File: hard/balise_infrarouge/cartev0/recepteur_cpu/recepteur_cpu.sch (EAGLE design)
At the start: 14 parts, among them U1 ARDUINO_SHIELDNO_SILK

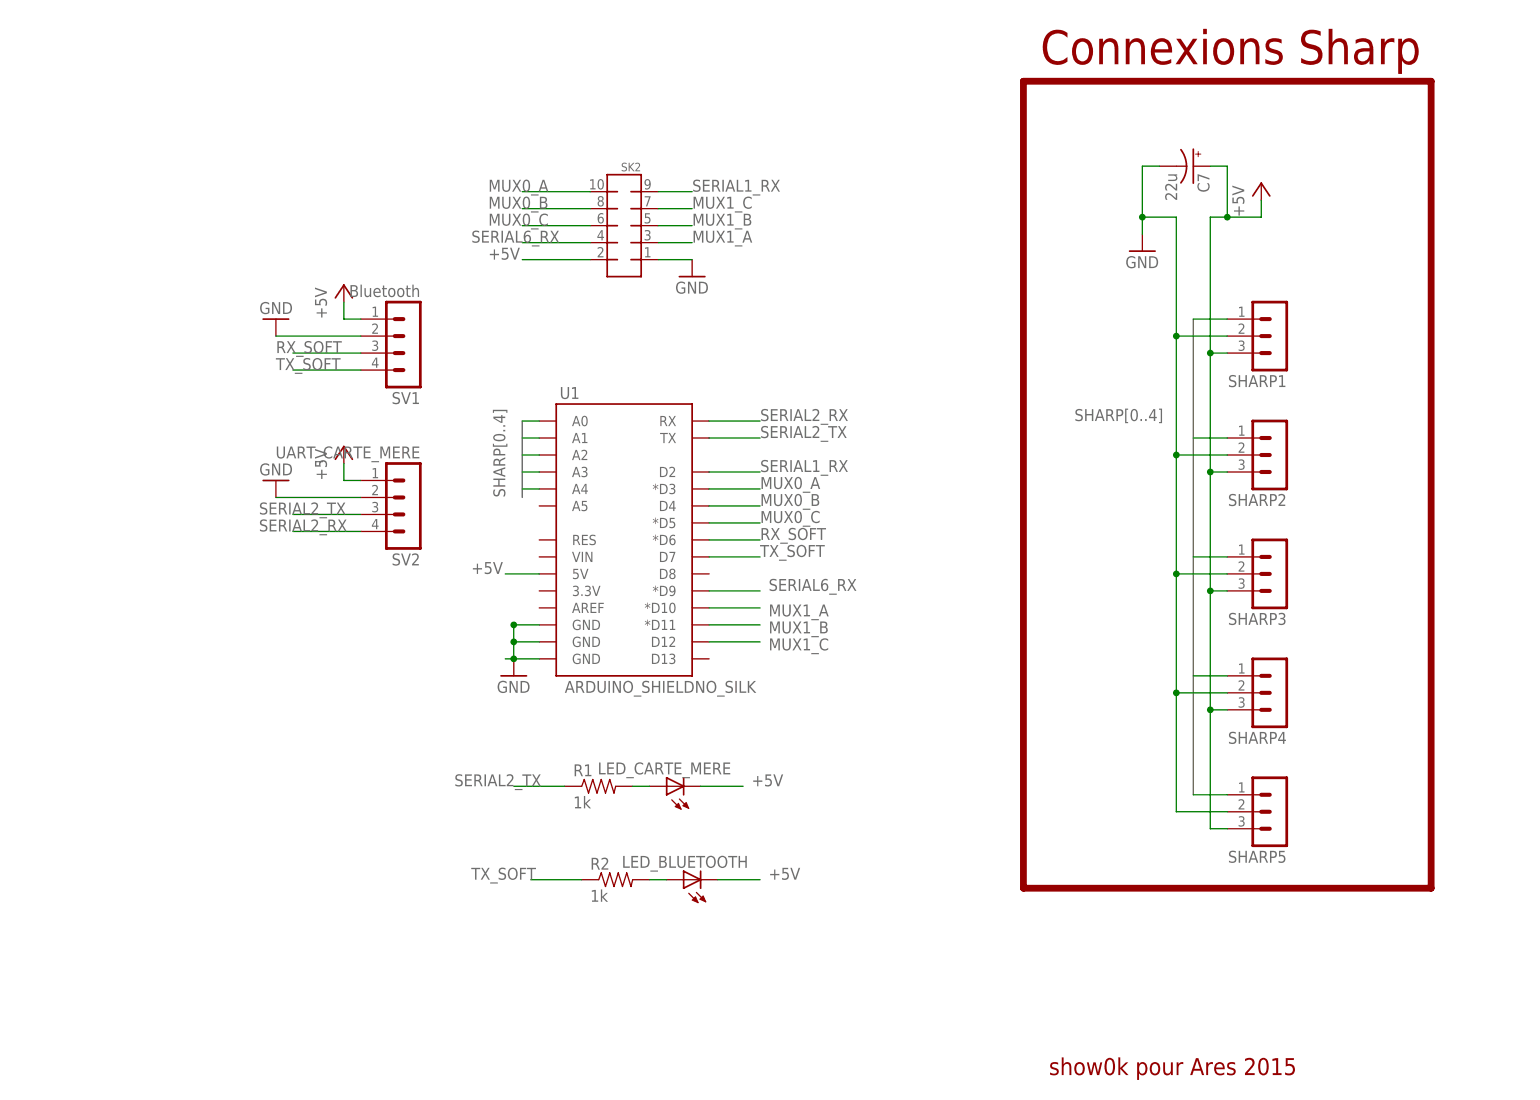
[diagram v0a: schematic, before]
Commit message: maj carte extension nucleo
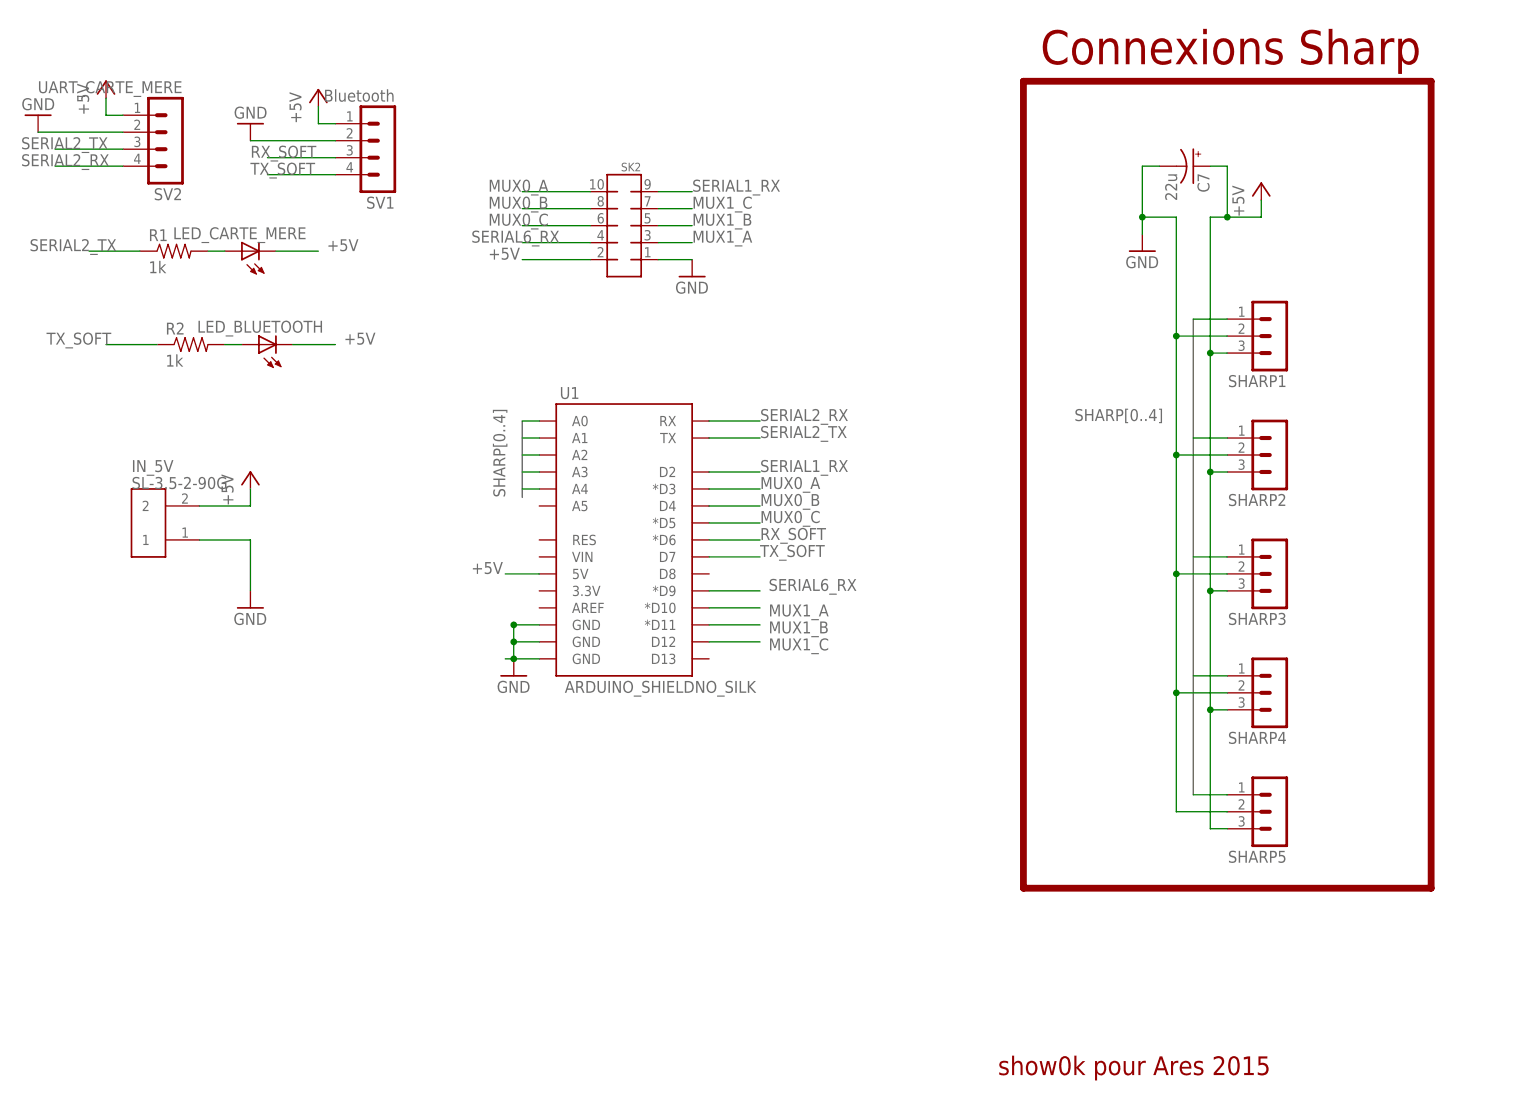
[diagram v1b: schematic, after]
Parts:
- added IN_5V: SL-3.5-2-90G, WEIDMULLER:SL-3.5-2-90G
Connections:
- net +5V: now also IN_5V.2
- net GND: now also IN_5V.1
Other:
- moved on the sheet: LED_BLUETOOTH, LED_CARTE_MERE, R1, R2, SV1, SV2
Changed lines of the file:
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@@
 <attribute name="OC_FARNELL" value="unknown"/>
 </part>
+<part name="IN_5V" library="WEIDMULLER" deviceset="SL-3.5-2-90G" device=""/>
+<part name="P+4" library="supply1" deviceset="+5V" device=""/>
+<part name="GND6" library="SparkFun-Aesthetics" deviceset="GND" device=""/>
 </parts>
 <sheets>
@@
 <wire x1="173.99" y1="-30.48" x2="173.99" y2="90.17" width="1.016" layer="94"/>
 <text x="176.53" y="92.71" size="5.08" layer="94">Connexions Sharp</text>
-<text x="177.8" y="-58.42" size="2.54" layer="94">show0k pour Ares 2015</text>
+<text x="170.18" y="-58.42" size="2.794" layer="94" font="vector" ratio="14">show0k pour Ares 2015</text>
 </plain>
 <instances>
@@
 <instance part="C7" gate="G$1" x="199.39" y="77.47" rot="R270"/>
 <instance part="P+3" gate="1" x="209.55" y="74.93"/>
-<instance part="SV1" gate="1" x="82.55" y="49.53" rot="R180"/>
-<instance part="P+10" gate="1" x="72.39" y="59.69"/>
-<instance part="GND1" gate="1" x="62.23" y="54.61" rot="R180"/>
+<instance part="SV1" gate="1" x="78.74" y="78.74" rot="R180"/>
+<instance part="P+10" gate="1" x="68.58" y="88.9"/>
+<instance part="GND1" gate="1" x="58.42" y="83.82" rot="R180"/>
 <instance part="GND2" gate="1" x="191.77" y="64.77"/>
 <instance part="GND3" gate="1" x="124.46" y="60.96"/>
 <instance part="GND4" gate="1" x="97.79" y="1.27"/>
-<instance part="SV2" gate="1" x="82.55" y="25.4" rot="R180"/>
-<instance part="P+1" gate="1" x="72.39" y="35.56"/>
-<instance part="GND5" gate="1" x="62.23" y="30.48" rot="R180"/>
-<instance part="LED_CARTE_MERE" gate="G$1" x="120.65" y="-15.24" smashed="yes" rot="R90">
-<attribute name="NAME" x="130.302" y="-11.684" size="1.778" layer="95" rot="R180"/>
-<attribute name="VALUE" x="122.682" y="-9.525" size="1.778" layer="96" rot="R180"/>
+<instance part="SV2" gate="1" x="46.99" y="80.01" rot="R180"/>
+<instance part="P+1" gate="1" x="36.83" y="90.17"/>
+<instance part="GND5" gate="1" x="26.67" y="85.09" rot="R180"/>
+<instance part="LED_CARTE_MERE" gate="G$1" x="57.15" y="64.77" smashed="yes" rot="R90">
+<attribute name="NAME" x="66.802" y="68.326" size="1.778" layer="95" rot="R180"/>
+<attribute name="VALUE" x="59.182" y="70.485" size="1.778" layer="96" rot="R180"/>
 </instance>
-<instance part="R1" gate="G$1" x="110.49" y="-15.24">
-<attribute name="OC_FARNELL" x="110.49" y="-12.7" size="1.778" layer="96" rot="R270" display="off"/>
-<attribute name="MF" x="110.49" y="-12.7" size="1.778" layer="96" rot="R270" display="off"/>
-<attribute name="MPN" x="110.49" y="-12.7" size="1.778" layer="96" rot="R270" display="off"/>
+<instance part="R1" gate="G$1" x="46.99" y="64.77">
+<attribute name="OC_FARNELL" x="46.99" y="67.31" size="1.778" layer="96" rot="R270" display="off"/>
+<attribute name="MF" x="46.99" y="67.31" size="1.778" layer="96" rot="R270" display="off"/>
+<attribute name="MPN" x="46.99" y="67.31" size="1.778" layer="96" rot="R270" display="off"/>
 </instance>
-<instance part="LED_BLUETOOTH" gate="G$1" x="123.19" y="-29.21" smashed="yes" rot="R90">
-<attribute name="NAME" x="132.842" y="-25.654" size="1.778" layer="95" rot="R180"/>
-<attribute name="VALUE" x="125.222" y="-23.495" size="1.778" layer="96" rot="R180"/>
+<instance part="LED_BLUETOOTH" gate="G$1" x="59.69" y="50.8" smashed="yes" rot="R90">
+<attribute name="NAME" x="69.342" y="54.356" size="1.778" layer="95" rot="R180"/>
+<attribute name="VALUE" x="61.722" y="56.515" size="1.778" layer="96" rot="R180"/>
 </instance>
-<instance part="R2" gate="G$1" x="113.03" y="-29.21">
-<attribute name="OC_FARNELL" x="113.03" y="-26.67" size="1.778" layer="96" rot="R270" display="off"/>
-<attribute name="MF" x="113.03" y="-26.67" size="1.778" layer="96" rot="R270" display="off"/>
-<attribute name="MPN" x="113.03" y="-26.67" size="1.778" layer="96" rot="R270" display="off"/>
+<instance part="R2" gate="G$1" x="49.53" y="50.8">
+<attribute name="OC_FARNELL" x="49.53" y="53.34" size="1.778" layer="96" rot="R270" display="off"/>
+<attribute name="MF" x="49.53" y="53.34" size="1.778" layer="96" rot="R270" display="off"/>
+<attribute name="MPN" x="49.53" y="53.34" size="1.778" layer="96" rot="R270" display="off"/>
 </instance>
+<instance part="IN_5V" gate="G$1" x="45.72" y="24.13"/>
+<instance part="P+4" gate="1" x="58.42" y="31.75"/>
+<instance part="GND6" gate="1" x="58.42" y="11.43"/>
 </instances>
 <busses>
@@
 <segment>
 <pinref part="SV2" gate="1" pin="4"/>
-<wire x1="64.77" y1="22.86" x2="74.93" y2="22.86" width="0.1524" layer="91"/>
-<label x="59.69" y="22.86" size="1.778" layer="95"/>
+<wire x1="29.21" y1="77.47" x2="39.37" y2="77.47" width="0.1524" layer="91"/>
+<label x="24.13" y="77.47" size="1.778" layer="95"/>
 </segment>
 </net>
@@
 <segment>
 <pinref part="SV2" gate="1" pin="3"/>
-<wire x1="64.77" y1="25.4" x2="74.93" y2="25.4" width="0.1524" layer="91"/>
-<label x="59.69" y="25.4" size="1.778" layer="95"/>
+<wire x1="29.21" y1="80.01" x2="39.37" y2="80.01" width="0.1524" layer="91"/>
+<label x="24.13" y="80.01" size="1.778" layer="95"/>
 </segment>
 <segment>
 <pinref part="R1" gate="G$1" pin="1"/>
-<wire x1="105.41" y1="-15.24" x2="97.79" y2="-15.24" width="0.1524" layer="91"/>
-<label x="88.9" y="-15.24" size="1.778" layer="95"/>
+<wire x1="41.91" y1="64.77" x2="34.29" y2="64.77" width="0.1524" layer="91"/>
+<label x="25.4" y="64.77" size="1.778" layer="95"/>
 </segment>
 </net>
@@
 <segment>
 <pinref part="SV1" gate="1" pin="2"/>
-<wire x1="62.23" y1="52.07" x2="74.93" y2="52.07" width="0.1524" layer="91"/>
+<wire x1="58.42" y1="81.28" x2="71.12" y2="81.28" width="0.1524" layer="91"/>
 <pinref part="GND1" gate="1" pin="GND"/>
 </segment>
@@
 <segment>
 <pinref part="SV2" gate="1" pin="2"/>
-<wire x1="62.23" y1="27.94" x2="74.93" y2="27.94" width="0.1524" layer="91"/>
+<wire x1="26.67" y1="82.55" x2="39.37" y2="82.55" width="0.1524" layer="91"/>
 <pinref part="GND5" gate="1" pin="GND"/>
+</segment>
+<segment>
+<pinref part="IN_5V" gate="G$1" pin="1"/>
+<wire x1="50.8" y1="21.59" x2="58.42" y2="21.59" width="0.1524" layer="91"/>
+<wire x1="58.42" y1="13.97" x2="58.42" y2="21.59" width="0.1524" layer="91"/>
+<pinref part="GND6" gate="1" pin="GND"/>
 </segment>
 </net>
@@
 <segment>
 <pinref part="P+10" gate="1" pin="+5V"/>
-<wire x1="72.39" y1="57.15" x2="72.39" y2="54.61" width="0.1524" layer="91"/>
+<wire x1="68.58" y1="86.36" x2="68.58" y2="83.82" width="0.1524" layer="91"/>
 <pinref part="SV1" gate="1" pin="1"/>
-<wire x1="72.39" y1="54.61" x2="74.93" y2="54.61" width="0.1524" layer="91"/>
+<wire x1="68.58" y1="83.82" x2="71.12" y2="83.82" width="0.1524" layer="91"/>
 </segment>
 <segment>
 <pinref part="P+1" gate="1" pin="+5V"/>
-<wire x1="72.39" y1="33.02" x2="72.39" y2="30.48" width="0.1524" layer="91"/>
+<wire x1="36.83" y1="87.63" x2="36.83" y2="85.09" width="0.1524" layer="91"/>
 <pinref part="SV2" gate="1" pin="1"/>
-<wire x1="72.39" y1="30.48" x2="74.93" y2="30.48" width="0.1524" layer="91"/>
+<wire x1="36.83" y1="85.09" x2="39.37" y2="85.09" width="0.1524" layer="91"/>
 </segment>
 <segment>
 <pinref part="LED_CARTE_MERE" gate="G$1" pin="C"/>
-<wire x1="125.73" y1="-15.24" x2="132.08" y2="-15.24" width="0.1524" layer="91"/>
-<label x="133.35" y="-15.24" size="1.778" layer="95"/>
+<wire x1="62.23" y1="64.77" x2="68.58" y2="64.77" width="0.1524" layer="91"/>
+<label x="69.85" y="64.77" size="1.778" layer="95"/>
 </segment>
 <segment>
 <pinref part="LED_BLUETOOTH" gate="G$1" pin="C"/>
-<wire x1="128.27" y1="-29.21" x2="134.62" y2="-29.21" width="0.1524" layer="91"/>
-<label x="135.89" y="-29.21" size="1.778" layer="95"/>
+<wire x1="64.77" y1="50.8" x2="71.12" y2="50.8" width="0.1524" layer="91"/>
+<label x="72.39" y="50.8" size="1.778" layer="95"/>
+</segment>
+<segment>
+<pinref part="IN_5V" gate="G$1" pin="2"/>
+<wire x1="50.8" y1="26.67" x2="58.42" y2="26.67" width="0.1524" layer="91"/>
+<wire x1="58.42" y1="26.67" x2="58.42" y2="29.21" width="0.1524" layer="91"/>
+<pinref part="P+4" gate="1" pin="+5V"/>
 </segment>
 </net>
@@
 <segment>
 <pinref part="SV1" gate="1" pin="3"/>
-<wire x1="64.77" y1="49.53" x2="74.93" y2="49.53" width="0.1524" layer="91"/>
-<label x="62.23" y="49.53" size="1.778" layer="95"/>
+<wire x1="60.96" y1="78.74" x2="71.12" y2="78.74" width="0.1524" layer="91"/>
+<label x="58.42" y="78.74" size="1.778" layer="95"/>
 </segment>
 <segment>
@@
 <segment>
 <pinref part="SV1" gate="1" pin="4"/>
-<wire x1="64.77" y1="46.99" x2="74.93" y2="46.99" width="0.1524" layer="91"/>
-<label x="62.23" y="46.99" size="1.778" layer="95"/>
+<wire x1="60.96" y1="76.2" x2="71.12" y2="76.2" width="0.1524" layer="91"/>
+<label x="58.42" y="76.2" size="1.778" layer="95"/>
 </segment>
 <segment>
@@
 <segment>
 <pinref part="R2" gate="G$1" pin="1"/>
-<wire x1="107.95" y1="-29.21" x2="100.33" y2="-29.21" width="0.1524" layer="91"/>
-<label x="91.44" y="-29.21" size="1.778" layer="95"/>
+<wire x1="44.45" y1="50.8" x2="36.83" y2="50.8" width="0.1524" layer="91"/>
+<label x="27.94" y="50.8" size="1.778" layer="95"/>
 </segment>
 </net>
@@
 <pinref part="R1" gate="G$1" pin="2"/>
 <pinref part="LED_CARTE_MERE" gate="G$1" pin="A"/>
-<wire x1="115.57" y1="-15.24" x2="118.11" y2="-15.24" width="0.1524" layer="91"/>
+<wire x1="52.07" y1="64.77" x2="54.61" y2="64.77" width="0.1524" layer="91"/>
 </segment>
 </net>
@@
 <pinref part="R2" gate="G$1" pin="2"/>
 <pinref part="LED_BLUETOOTH" gate="G$1" pin="A"/>
-<wire x1="118.11" y1="-29.21" x2="120.65" y2="-29.21" width="0.1524" layer="91"/>
-</segment>
-</net>
+<wire x1="54.61" y1="50.8" x2="57.15" y2="50.8" width="0.1524" layer="91"/>
+</segment>
+</net>
